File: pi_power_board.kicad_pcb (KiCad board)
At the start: 2 copper layers, 34.8 x 23.1 mm, 26 parts, among them J1 381camcon, J2 Conn_02x04_Odd_Even, Q1 SSM3K335R, Q2 SSM3K335R, Q3 DMG2305UX-7, U1 LM74610, U2 TPS2400, U3 DMMT5401

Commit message: Add files via upload
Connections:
- D1 pad 1: Net-(D1-Pad1) -> +VDC
- F1 pad 2: Net-(D1-Pad1) -> Net-(F1-Pad2)
- J1 pad 1: Net-(D1-Pad1) -> Net-(F1-Pad2)
- J2 pad 1: (no net) -> Net-(J2-Pad1)
- U1 pad 3: (no net) -> Net-(U1-Pad3)
- U1 pad 5: (no net) -> Net-(U1-Pad5)
- U2 pad 1: (no net) -> Net-(U2-Pad1)
- U2 pad 3: (no net) -> Net-(U2-Pad3)
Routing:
- removed copper zone on F.Cu, net GND
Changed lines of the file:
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@@
     (thickness 1.6)
     (drawings 15)
-    (tracks 130)
+    (tracks 129)
     (zones 0)
     (modules 26)
-    (nets 24)
+    (nets 30)
   )
   (page A4)
@@
   )
   (setup
-    (last_trace_width 0.254)
+    (last_trace_width 0.508)
     (user_trace_width 0.381)
     (user_trace_width 0.508)
@@
   (net 22 "Net-(LED1-Pad4)")
   (net 23 "Net-(R7-Pad1)")
+  (net 24 "Net-(F1-Pad2)")
+  (net 25 "Net-(J2-Pad1)")
+  (net 26 "Net-(U1-Pad3)")
+  (net 27 "Net-(U1-Pad5)")
+  (net 28 "Net-(U2-Pad1)")
+  (net 29 "Net-(U2-Pad3)")
   (net_class Default "This is the default net class."
     (clearance 0.127)
@@
     (add_net "Net-(D5-Pad1)")
     (add_net "Net-(D5-Pad2)")
+    (add_net "Net-(F1-Pad2)")
+    (add_net "Net-(J2-Pad1)")
     (add_net "Net-(LED1-Pad2)")
     (add_net "Net-(LED1-Pad4)")
@@
     (add_net "Net-(R3-Pad1)")
     (add_net "Net-(R7-Pad1)")
+    (add_net "Net-(U1-Pad3)")
+    (add_net "Net-(U1-Pad5)")
+    (add_net "Net-(U2-Pad1)")
+    (add_net "Net-(U2-Pad3)")
   )
   (module DMMT5401:DMMT5401 (layer F.Cu)
@@
       (net 4 GND))
     (pad 1 thru_hole circle (at -1.905 -4) (size 1.2 1.2) (drill 0.762) (layers *.Cu *.Mask)
-      (net 14 "Net-(D1-Pad1)"))
+      (net 24 "Net-(F1-Pad2)"))
   )
   (module APHBM2012:APHBM2012 (layer F.Cu)
@@
       (net 17 "Net-(Q1-Pad1)") (solder_mask_margin 0.05) (clearance 0.127))
     (pad 3 smd rect (at 0.3 2.1) (size 0.45 1.45) (drill (offset 0.025 0.025)) (layers F.Cu F.Adhes F.Paste F.SilkS F.Mask)
-      (solder_mask_margin 0.05) (clearance 0.127))
+      (net 26 "Net-(U1-Pad3)") (solder_mask_margin 0.05) (clearance 0.127))
     (pad 4 smd rect (at 0.95 2.1) (size 0.45 1.45) (drill (offset 0.025 0.025)) (layers F.Cu F.Adhes F.Paste F.SilkS F.Mask)
       (net 3 +VDC) (solder_mask_margin 0.05) (clearance 0.127))
@@
       (net 17 "Net-(Q1-Pad1)") (solder_mask_margin 0.05) (clearance 0.127))
     (pad 5 smd rect (at 0.95 -2.35) (size 0.45 1.45) (drill (offset 0.025 0.025)) (layers F.Cu F.Adhes F.Paste F.SilkS F.Mask)
-      (solder_mask_margin 0.05) (clearance 0.127))
+      (net 27 "Net-(U1-Pad5)") (solder_mask_margin 0.05) (clearance 0.127))
   )
   (module Package_TO_SOT_SMD:SOT-23 (layer F.Cu)
@@
     (fp_line (start 0.9 1.55) (end -0.9 1.55) (layer F.Fab) (width 0.1))
     (fp_line (start 0.9 -1.55) (end 0.9 1.55) (layer F.Fab) (width 0.1))
-    (pad 1 smd rect (at -1.1 -0.95 270) (size 1.06 0.65) (layers F.Cu F.Paste F.Mask))
+    (pad 1 smd rect (at -1.1 -0.95 270) (size 1.06 0.65) (layers F.Cu F.Paste F.Mask)
+      (net 28 "Net-(U2-Pad1)"))
     (pad 2 smd rect (at -1.1 0 270) (size 1.06 0.65) (layers F.Cu F.Paste F.Mask)
       (net 4 GND))
-    (pad 3 smd rect (at -1.1 0.95 270) (size 1.06 0.65) (layers F.Cu F.Paste F.Mask))
+    (pad 3 smd rect (at -1.1 0.95 270) (size 1.06 0.65) (layers F.Cu F.Paste F.Mask)
+      (net 29 "Net-(U2-Pad3)"))
     (pad 4 smd rect (at 1.1 0.95 270) (size 1.06 0.65) (layers F.Cu F.Paste F.Mask)
       (net 18 "Net-(Q2-Pad1)"))
@@
     (pad 2 thru_hole oval (at 2.54 0) (size 1.7 1.7) (drill 1) (layers *.Cu *.Mask)
       (net 13 +5V))
-    (pad 1 thru_hole rect (at 0 0) (size 1.7 1.7) (drill 1) (layers *.Cu *.Mask))
+    (pad 1 thru_hole rect (at 0 0) (size 1.7 1.7) (drill 1) (layers *.Cu *.Mask)
+      (net 25 "Net-(J2-Pad1)"))
     (model ${KISYS3DMOD}/Connector_PinHeader_2.54mm.3dshapes/PinHeader_2x04_P2.54mm_Vertical.wrl
       (at (xyz 0 0 0))
@@
     (fp_line (start -2.25 1.6) (end -2.25 -1.6) (layer F.Fab) (width 0.1))
     (pad 2 smd roundrect (at 2.225 0) (size 1.3 3.4) (layers F.Cu F.Paste F.Mask) (roundrect_rratio 0.192308)
-      (net 14 "Net-(D1-Pad1)"))
+      (net 24 "Net-(F1-Pad2)"))
     (pad 1 smd roundrect (at -2.225 0) (size 1.3 3.4) (layers F.Cu F.Paste F.Mask) (roundrect_rratio 0.192308)
       (net 3 +VDC))
@@
       (net 4 GND))
     (pad 1 smd rect (at -0.7 0 90) (size 0.6 0.7) (layers F.Cu F.Paste F.Mask)
-      (net 14 "Net-(D1-Pad1)"))
+      (net 3 +VDC))
     (model ${KISYS3DMOD}/Diode_SMD.3dshapes/D_SOD-523.wrl
       (at (xyz 0 0 0))
@@
   (segment (start 94.50349 131.575212) (end 94.50349 126.08401) (width 0.889) (layer F.Cu) (net 13))
   (segment (start 92.567702 133.511) (end 94.50349 131.575212) (width 0.889) (layer F.Cu) (net 13))
-  (segment (start 89.725 133.511) (end 92.567702 133.511) (width 0.889) (layer F.Cu) (net 13))
-  (segment (start 89.575 133.661) (end 89.725 133.511) (width 0.889) (layer F.Cu) (net 13))
-  (segment (start 89.575 135) (end 89.575 133.661) (width 0.889) (layer F.Cu) (net 13))
-  (segment (start 89.217001 134.018999) (end 88.981001 134.018999) (width 0.508) (layer F.Cu) (net 13))
-  (segment (start 89.575 133.661) (end 89.217001 134.018999) (width 0.508) (layer F.Cu) (net 13))
-  (segment (start 88.981001 134.018999) (end 89.118999 134.018999) (width 0.508) (layer F.Cu) (net 13))
   (segment (start 85.25 134.764198) (end 85.25 135.15) (width 0.508) (layer F.Cu) (net 13))
-  (segment (start 85.995199 134.018999) (end 85.25 134.764198) (width 0.508) (layer F.Cu) (net 13))
-  (segment (start 88.981001 134.018999) (end 85.995199 134.018999) (width 0.508) (layer F.Cu) (net 13))
+  (segment (start 91.014 133.511) (end 89.575 134.95) (width 0.889) (layer F.Cu) (net 13))
+  (segment (start 92.567702 133.511) (end 91.014 133.511) (width 0.889) (layer F.Cu) (net 13))
+  (segment (start 89.575 134.95) (end 89.575 135) (width 0.508) (layer F.Cu) (net 13))
+  (segment (start 88.667 134.042) (end 89.575 134.95) (width 0.508) (layer F.Cu) (net 13))
+  (segment (start 86.091573 134.042) (end 88.667 134.042) (width 0.508) (layer F.Cu) (net 13))
+  (segment (start 85.25 134.883573) (end 86.091573 134.042) (width 0.508) (layer F.Cu) (net 13))
+  (segment (start 85.25 135.15) (end 85.25 134.883573) (width 0.508) (layer F.Cu) (net 13))
   (segment (start 96.675 117.7) (end 96.95 117.7) (width 0.889) (layer F.Cu) (net 14))
   (segment (start 95.275 119.1) (end 96.675 117.7) (width 0.889) (layer F.Cu) (net 14))
@@
       )
     )
-  )
-  (zone (net 4) (net_name GND) (layer F.Cu) (hatch edge 0.508)
-    (connect_pads (clearance 0.127))
-    (min_thickness 0.254)
-    (fill yes (arc_segments 32) (thermal_gap 0.381) (thermal_bridge_width 0.381))
-    (polygon
-      (pts
-        (xy 82.7 115.85) (xy 101.9 115.85) (xy 103.65 117.6) (xy 117.05 117.6) (xy 117.05 127.2)
-        (xy 105.55 127.2) (xy 105.55 138.6) (xy 82.7 138.6)
-      )
-    )

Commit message: Add files via upload
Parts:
- moved D1 6.24 mm to (90.8, 117.3), turned to 90 degrees
- moved F1 1.95 mm to (95.0, 119.0)
- moved J1 1.00 mm to (113.0, 129.6)
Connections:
- J2 pad 1: Net-(J2-Pad1) -> (no net)
- U1 pad 3: Net-(U1-Pad3) -> (no net)
- U1 pad 5: Net-(U1-Pad5) -> (no net)
- U2 pad 1: Net-(U2-Pad1) -> (no net)
- U2 pad 3: Net-(U2-Pad3) -> (no net)
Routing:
- net Net-(D1-Pad1): track 23.6 -> 0.00 mm
- net Net-(F1-Pad2): track 0.00 -> 18.1 mm
- net +VDC: track 17.5 -> 18.2 mm
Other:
- board size 34.8 x 23.1 mm -> 34.8 x 24 mm
- board text added: "+5V"
- board text added: "GND"

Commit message: Add files via upload
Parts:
- D1: value D5V0L1B2T-7 -> ESDA18-1K
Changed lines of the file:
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@@
   )
   (setup
-    (last_trace_width 0.889)
+    (last_trace_width 0.254)
     (user_trace_width 0.381)
     (user_trace_width 0.508)
@@
       (effects (font (size 1 1) (thickness 0.15)))
     )
-    (fp_text value D5V0L1B2T-7 (at 0 1.4 90) (layer F.Fab)
-      (effects (font (size 1 1) (thickness 0.15)))
-    )
+    (fp_text value ESDA18-1K (at 0 1.4 90) (layer F.Fab)
+      (effects (font (size 1 1) (thickness 0.15)))
+    )

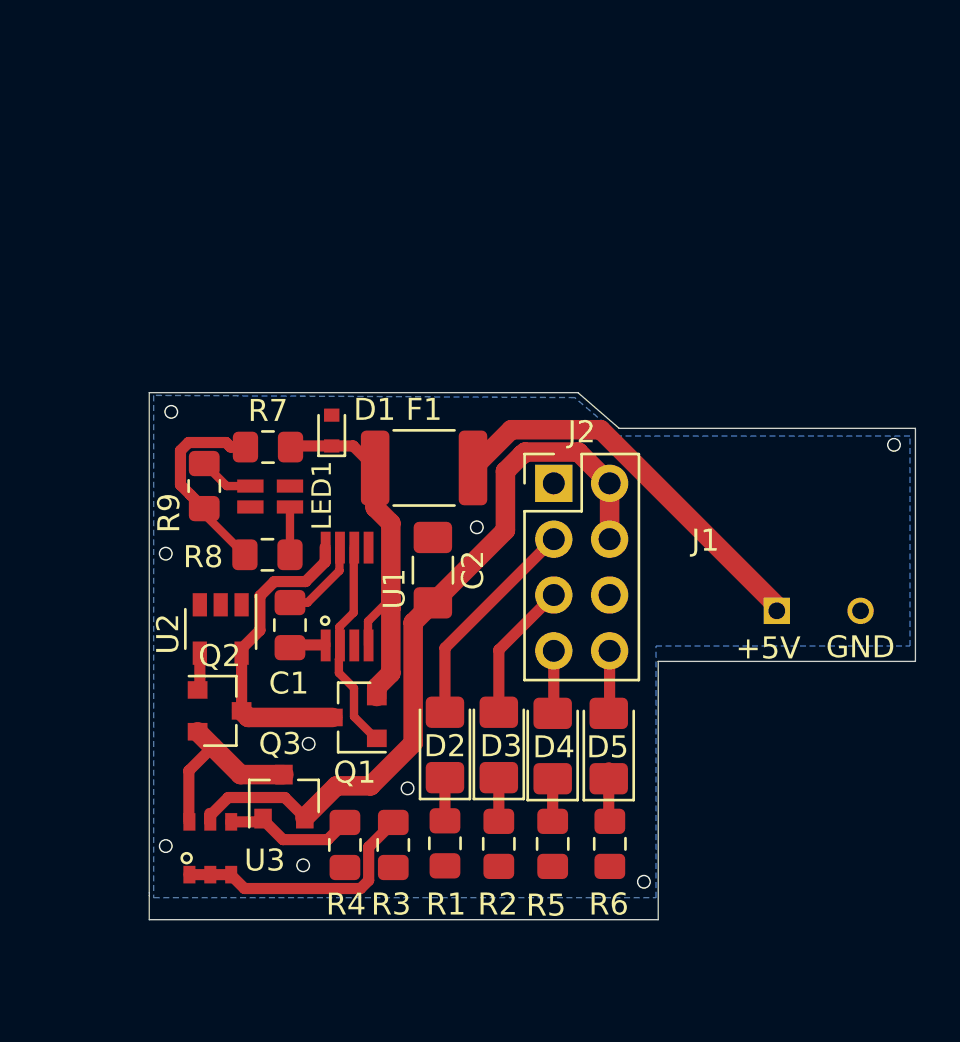
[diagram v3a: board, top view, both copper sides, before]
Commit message: Change header to SMT W/through holes
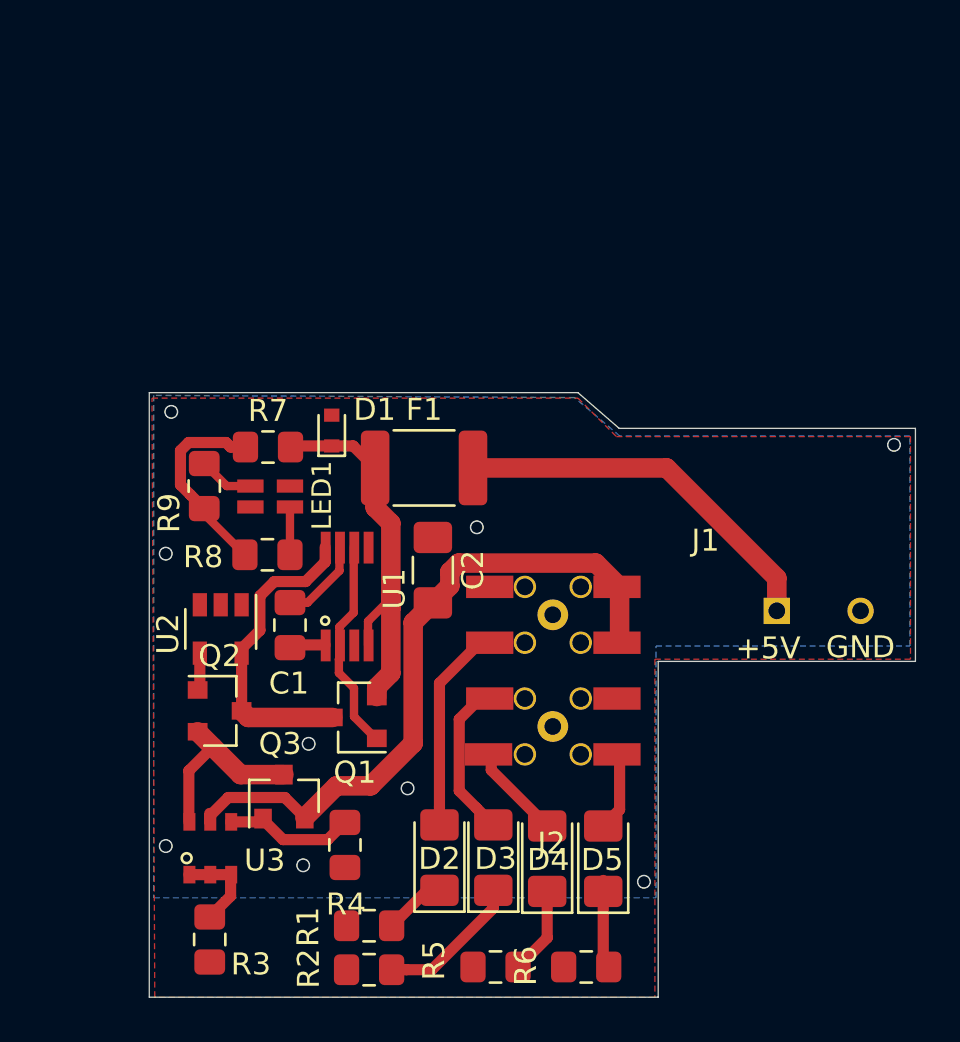
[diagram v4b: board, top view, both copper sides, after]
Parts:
- J2: footprint Connector_PinHeader_2.54mm:PinHeader_2x04_P2.54mm_Vertical -> BG120-08-A-0-N-D:BG120-08-A-0-N-D
- moved R3 9.39 mm to (85.2, 140.5)
- moved J2 9.00 mm to (100.8, 128.8)
- moved R2 8.22 mm to (92.5, 141.9), turned to 180 degrees
- moved R5 6.17 mm to (98.2, 141.8), turned to 180 degrees
- moved R6 5.70 mm to (102.4, 141.8), turned to 180 degrees
- moved D2 5.13 mm to (95.7, 136.8)
- moved D3 5.13 mm to (98.2, 136.8)
- moved D4 5.13 mm to (100.6, 136.8)
- moved D5 5.13 mm to (103.2, 136.8)
- moved R1 5.10 mm to (92.5, 139.9), turned to 180 degrees
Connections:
- J2 pad 1: (no net) -> Net-(J2-Pad1)
- U1 pad 3: (no net) -> Net-(U1-Pad3)
- U1 pad 5: (no net) -> Net-(U1-Pad5)
- U2 pad 1: (no net) -> Net-(U2-Pad1)
- U2 pad 3: (no net) -> Net-(U2-Pad3)
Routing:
- net Net-(R3-Pad1): track 11.7 -> 4.22 mm
- net Net-(D3-Pad1): track 1.99 -> 6.60 mm
- net +5V: track 34.4 -> 31.4 mm
- net Net-(D4-Pad1): track 1.94 -> 3.99 mm
- net Net-(D5-Pad1): track 2.03 -> 3.61 mm
- net Net-(D4-Pad2): track 2.86 -> 4.38 mm
- net Net-(D3-Pad2): track 6.37 -> 7.56 mm
- net Net-(D2-Pad1): track 1.96 -> 2.84 mm
- net Net-(D5-Pad2): track 2.86 -> 3.62 mm
- net GND: track 0.64 -> 0.00 mm
- added copper zone on F.Cu, net GND
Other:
- board size 34.8 x 24 mm -> 34.8 x 27.5 mm

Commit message: Manufacturability changes and dimension fixing
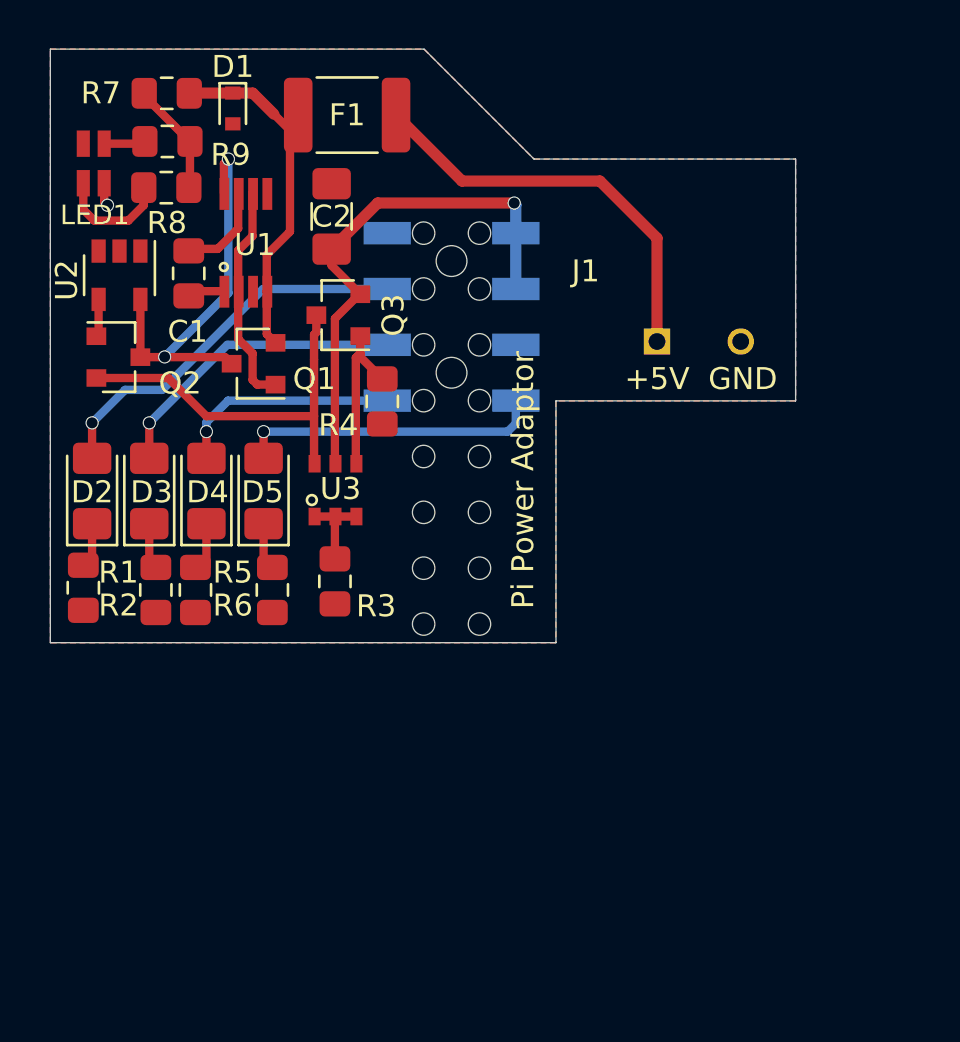
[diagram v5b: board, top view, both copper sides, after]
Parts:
- moved D2 23.0 mm to (79.9, 120.1)
- moved D3 22.9 mm to (82.5, 120.1)
- moved D4 22.8 mm to (85.1, 120.1)
- moved D5 22.8 mm to (87.7, 120.1)
- moved R6 22.3 mm to (88.1, 124.6), turned to 270 degrees
- moved Q3 22.0 mm to (91.1, 112.1), turned to 180 degrees
- moved R5 21.9 mm to (84.6, 124.6), turned to 270 degrees
- moved LED1 21.1 mm to (77.7, 103.2), turned to 90 degrees
- moved R4 20.2 mm to (93.1, 116.0)
- moved R1 20.1 mm to (79.5, 124.5), turned to 270 degrees
- moved R2 19.8 mm to (82.8, 124.6), turned to 270 degrees
- moved R8 17.3 mm to (83.3, 106.3), turned to 0 degrees
- moved R3 17.3 mm to (90.9, 124.2)
- moved U3 17.3 mm to (91.1, 119.8)
- moved J2 17.2 mm to (96.2, 112.2)
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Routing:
- net Net-(D5-Pad2): track 3.62 -> 13.9 mm, vias 0 -> 1
- net Net-(Q2-Pad2): track 8.60 -> 17.4 mm
- net Net-(D2-Pad2): track 9.61 -> 17.6 mm, vias 0 -> 1
- net +5V: track 31.4 -> 23.9 mm, vias 0 -> 1
- net Net-(D3-Pad2): track 7.56 -> 13.9 mm, vias 0 -> 1
- net Net-(D4-Pad2): track 4.38 -> 10.3 mm, vias 0 -> 1
- net Net-(D3-Pad1): track 6.60 -> 1.99 mm
- net Net-(Q1-Pad3): track 14.2 -> 18.7 mm, vias 0 -> 2
- net Net-(R7-Pad1): track 9.39 -> 5.17 mm
- net Net-(LED1-Pad2): track 2.17 -> 5.25 mm
- net +VDC: track 18.2 -> 15.6 mm
- net Net-(D4-Pad1): track 3.99 -> 1.99 mm
- net Net-(D5-Pad1): track 3.61 -> 1.99 mm
- net Net-(F1-Pad2): track 17.6 -> 18.9 mm
- net GND: track 0.00 -> 1.06 mm, vias 9 -> 1
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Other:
- board size 34.8 x 27.5 mm -> 33.9 x 27 mm
- board text added: "Pi Power Adaptor"
- board text added: "r1.0"
